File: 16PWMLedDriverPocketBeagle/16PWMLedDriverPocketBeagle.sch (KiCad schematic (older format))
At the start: 16 parts, among them J1 RJ45, J2 RJ45, P1 POCKETBEAGLE-P1, P2 POCKETBEAGLE-P2, T1 + 15 in -, T2 + 15 out -, U1 TCAN332DR, U2 SN65HVD233-HT

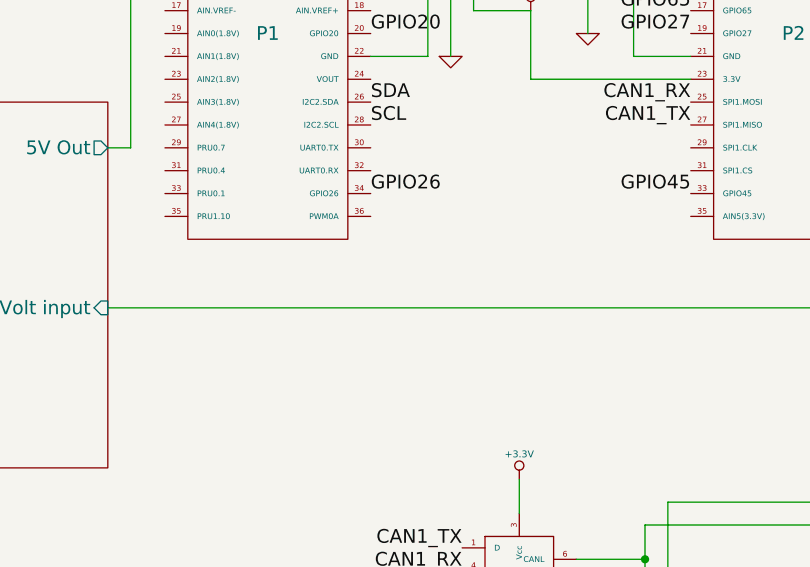
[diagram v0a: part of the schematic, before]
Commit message: Convert the 16PWM Led Drivers to use 12V for the LEDs.
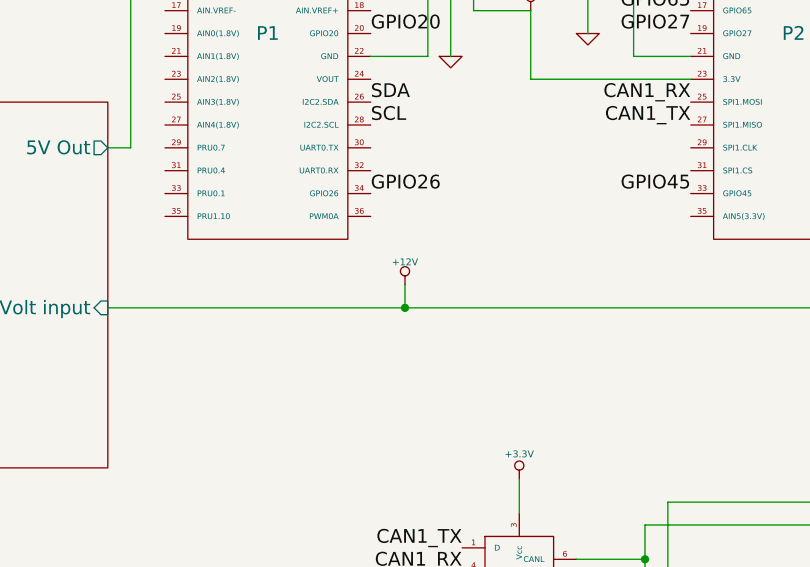
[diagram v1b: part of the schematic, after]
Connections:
- net Power Supply/12-15 Volt input renamed +12V
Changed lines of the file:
@@
 Sheet 1 3
 Title ""
-Date "11 mar 2019"
+Date "28 mar 2019"
 Rev ""
 Comp ""
@@
 	2300 1500 2300 1650
 Connection ~ 2300 1650
+$Comp
+L +12V #PWR014
+U 1 1 5C9CC877
+P 3450 3650
+F 0 "#PWR014" H 3450 3600 20  0001 C CNN
+F 1 "+12V" H 3450 3750 30  0000 C CNN
+F 2 "" H 3450 3650 60  0000 C CNN
+F 3 "" H 3450 3650 60  0000 C CNN
+	1    3450 3650
+	1    0    0    -1
+$EndComp
+Wire Wire Line
+	3450 3650 3450 3750
+Connection ~ 3450 3750
 $EndSCHEMATC

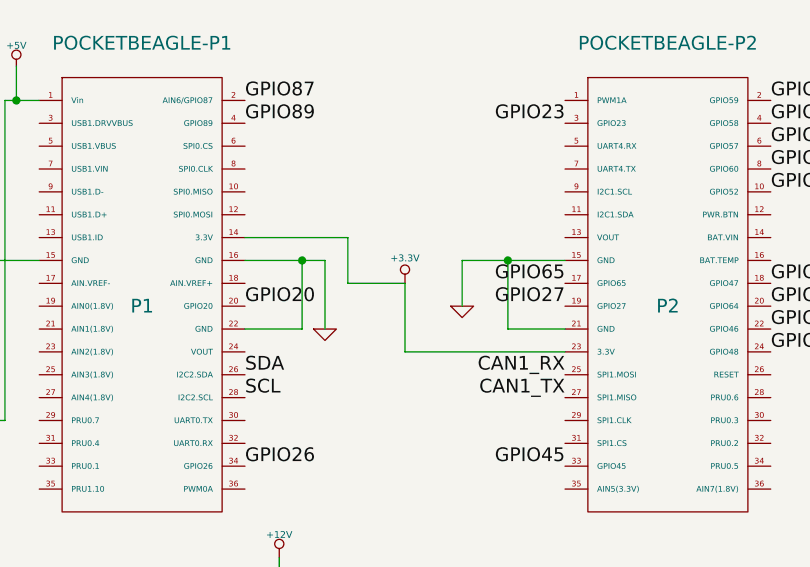
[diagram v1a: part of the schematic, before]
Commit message: Move Pocket Beagle SDA usage from I2C2 to I2C1 (reserved I2C for eeprom?).
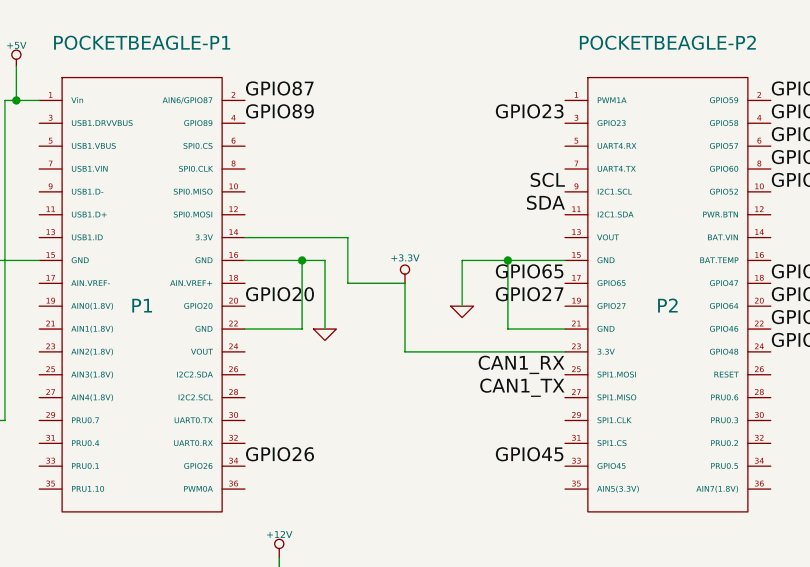
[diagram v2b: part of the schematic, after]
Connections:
- net SCL: now also P2.9 (I2C1.SCL); no longer P1.28 (I2C2.SCL)
- net SDA: now also P2.11 (I2C1.SDA); no longer P1.26 (I2C2.SDA)
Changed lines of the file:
@@
 Sheet 1 3
 Title ""
-Date "28 mar 2019"
+Date "5 jul 2019"
 Rev ""
 Comp ""
@@
 F4 "OE" I L 1700 6850 60
 $EndSheet
-Text Label 3300 2850 0    60   ~ 0
+Text Label 4700 2150 2    60   ~ 0
 SDA
-Text Label 3300 2950 0    60   ~ 0
+Text Label 4700 2050 2    60   ~ 0
 SCL
 Text Label 1700 6300 2    60   ~ 0

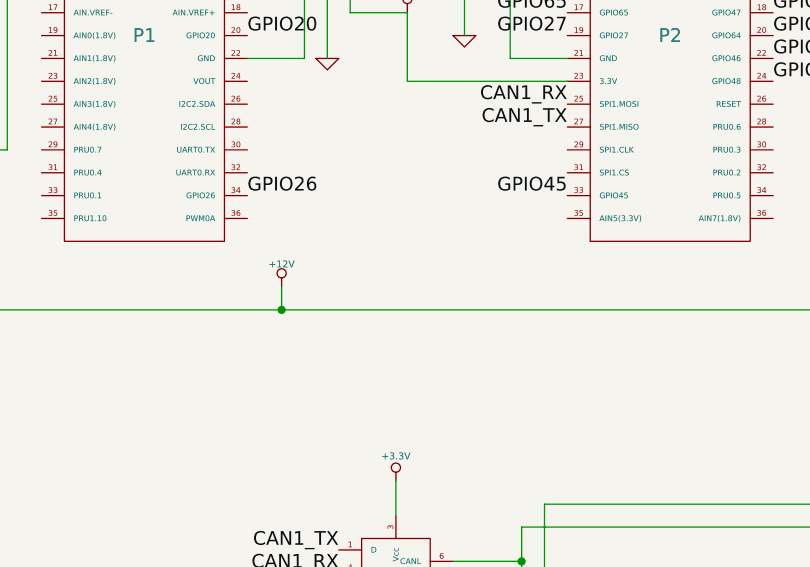
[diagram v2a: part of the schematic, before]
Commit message: Remove unused DIP and add LED power terminals.
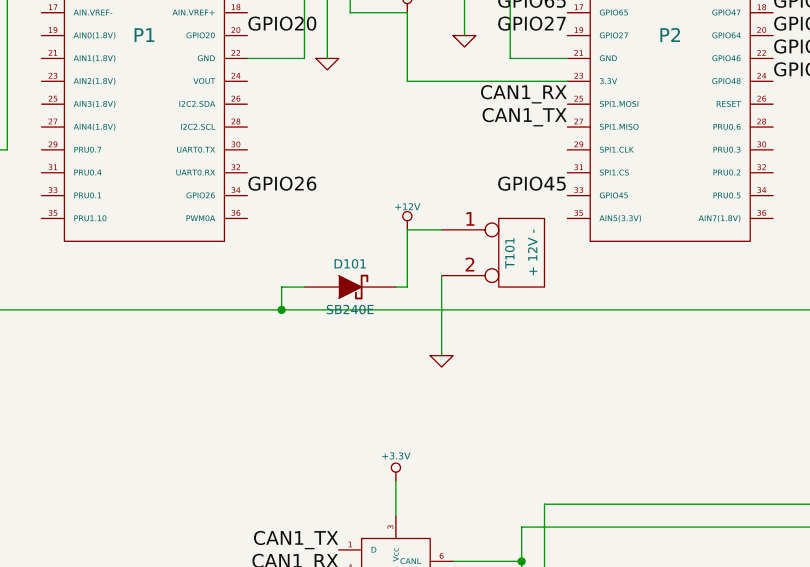
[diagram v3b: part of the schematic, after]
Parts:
- added D101: SB240E, ~, symbol DIODESCH
- added T101: + 12V -, ~, symbol CONN_2
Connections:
- net +12V: now also D101.2 (K), T101.1 (P1); no longer D1.2 (K), D2.1 (A), J1.8, J2.8
- net GND: now also T101.2 (PM)
- new net Power Supply/12-15 Volt input: D1.2 (K), D101.1 (A), D2.1 (A), J1.8, J2.8
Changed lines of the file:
@@
 Sheet 1 3
 Title ""
-Date "5 jul 2019"
+Date "30 jan 2020"
 Rev ""
 Comp ""
@@
 CAN1_TX
 $Comp
-L +3.3V #PWR01
+L +3.3V #PWR108
 U 1 1 5C7C3FF9
 P 4000 2450
-F 0 "#PWR01" H 4000 2410 30  0001 C CNN
+F 0 "#PWR108" H 4000 2410 30  0001 C CNN
 F 1 "+3.3V" H 4000 2560 30  0000 C CNN
 F 2 "" H 4000 2450 60  0000 C CNN
@@
 $EndComp
 $Comp
-L GND #PWR02
+L GND #PWR103
 U 1 1 5C7C401B
 P 3650 2650
-F 0 "#PWR02" H 3650 2650 30  0001 C CNN
+F 0 "#PWR103" H 3650 2650 30  0001 C CNN
 F 1 "GND" H 3650 2580 30  0001 C CNN
 F 2 "" H 3650 2650 60  0000 C CNN
@@
 $EndComp
 $Comp
-L GND #PWR03
+L GND #PWR111
 U 1 1 5C7C4038
 P 4250 2550
-F 0 "#PWR03" H 4250 2550 30  0001 C CNN
+F 0 "#PWR111" H 4250 2550 30  0001 C CNN
 F 1 "GND" H 4250 2480 30  0001 C CNN
 F 2 "" H 4250 2550 60  0000 C CNN
@@
 $EndComp
 $Comp
-L GND #PWR04
+L GND #PWR101
 U 1 1 5C7C406F
 P 2050 2350
-F 0 "#PWR04" H 2050 2350 30  0001 C CNN
+F 0 "#PWR101" H 2050 2350 30  0001 C CNN
 F 1 "GND" H 2050 2280 30  0001 C CNN
 F 2 "" H 2050 2350 60  0000 C CNN
@@
 $EndComp
 $Comp
-L GND #PWR05
+L GND #PWR114
 U 1 1 5C7C42F0
 P 7000 2350
-F 0 "#PWR05" H 7000 2350 30  0001 C CNN
+F 0 "#PWR114" H 7000 2350 30  0001 C CNN
 F 1 "GND" H 7000 2280 30  0001 C CNN
 F 2 "" H 7000 2350 60  0000 C CNN
@@
 CAN1_RX
 $Comp
-L GND #PWR06
+L GND #PWR107
 U 1 1 5C7C44D6
 P 3950 6600
-F 0 "#PWR06" H 3950 6600 30  0001 C CNN
+F 0 "#PWR107" H 3950 6600 30  0001 C CNN
 F 1 "GND" H 3950 6530 30  0001 C CNN
 F 2 "" H 3950 6600 60  0000 C CNN
@@
 $EndComp
 $Comp
-L +3.3V #PWR07
+L +3.3V #PWR106
 U 1 1 5C7C44E5
 P 3950 5650
-F 0 "#PWR07" H 3950 5610 30  0001 C CNN
+F 0 "#PWR106" H 3950 5610 30  0001 C CNN
 F 1 "+3.3V" H 3950 5760 30  0000 C CNN
 F 2 "" H 3950 5650 60  0000 C CNN
@@
 $EndComp
 $Comp
-L +3.3V #PWR08
+L +3.3V #PWR104
 U 1 1 5C7C44F4
 P 3950 4500
-F 0 "#PWR08" H 3950 4460 30  0001 C CNN
+F 0 "#PWR104" H 3950 4460 30  0001 C CNN
 F 1 "+3.3V" H 3950 4610 30  0000 C CNN
 F 2 "" H 3950 4500 60  0000 C CNN
@@
 $EndComp
 $Comp
-L GND #PWR09
+L GND #PWR105
 U 1 1 5C7C4503
 P 3950 5450
-F 0 "#PWR09" H 3950 5450 30  0001 C CNN
+F 0 "#PWR105" H 3950 5450 30  0001 C CNN
 F 1 "GND" H 3950 5380 30  0001 C CNN
 F 2 "" H 3950 5450 60  0000 C CNN
@@
 	4800 5650 5200 5650
 $Comp
-L +3.3V #PWR010
+L +3.3V #PWR112
 U 1 1 5C7C4768
 P 5000 5150
-F 0 "#PWR010" H 5000 5110 30  0001 C CNN
+F 0 "#PWR112" H 5000 5110 30  0001 C CNN
 F 1 "+3.3V" H 5000 5260 30  0000 C CNN
 F 2 "" H 5000 5150 60  0000 C CNN
@@
 $EndComp
 $Comp
-L GND #PWR011
+L GND #PWR113
 U 1 1 5C7C4777
 P 5000 5750
-F 0 "#PWR011" H 5000 5750 30  0001 C CNN
+F 0 "#PWR113" H 5000 5750 30  0001 C CNN
 F 1 "GND" H 5000 5680 30  0001 C CNN
 F 2 "" H 5000 5750 60  0000 C CNN
@@
 $EndComp
 $Comp
-L GND #PWR012
+L GND #PWR115
 U 1 1 5C7C488B
 P 7400 6450
-F 0 "#PWR012" H 7400 6450 30  0001 C CNN
+F 0 "#PWR115" H 7400 6450 30  0001 C CNN
 F 1 "GND" H 7400 6380 30  0001 C CNN
 F 2 "" H 7400 6450 60  0000 C CNN
@@
 GPIO89
 $Comp
-L +5V #PWR013
+L +5V #PWR102
 U 1 1 5C85AC7C
 P 2300 1500
-F 0 "#PWR013" H 2300 1590 20  0001 C CNN
+F 0 "#PWR102" H 2300 1590 20  0001 C CNN
 F 1 "+5V" H 2300 1590 30  0000 C CNN
 F 2 "" H 2300 1500 60  0000 C CNN
@@
 Connection ~ 2300 1650
 $Comp
-L +12V #PWR014
+L +12V #PWR109
 U 1 1 5C9CC877
-P 3450 3650
-F 0 "#PWR014" H 3450 3600 20  0001 C CNN
-F 1 "+12V" H 3450 3750 30  0000 C CNN
-F 2 "" H 3450 3650 60  0000 C CNN
-F 3 "" H 3450 3650 60  0000 C CNN
-	1    3450 3650
+P 4000 3400
+F 0 "#PWR109" H 4000 3350 20  0001 C CNN
+F 1 "+12V" H 4000 3500 30  0000 C CNN
+F 2 "" H 4000 3400 60  0000 C CNN
+F 3 "" H 4000 3400 60  0000 C CNN
+	1    4000 3400
 	1    0    0    -1
 $EndComp
@@
 	3450 3650 3450 3750
 Connection ~ 3450 3750
+$Comp
+L DIODESCH D101
+U 1 1 5E333922
+P 3750 3650
+F 0 "D101" H 3750 3750 40  0000 C CNN
+F 1 "SB240E" H 3750 3550 40  0000 C CNN
+F 2 "~" H 3750 3650 60  0000 C CNN
+F 3 "~" H 3750 3650 60  0000 C CNN
+	1    3750 3650
+	1    0    0    -1
+$EndComp
+Wire Wire Line
+	3450 3650 3550 3650
+Wire Wire Line
+	4000 3650 3950 3650
+Wire Wire Line
+	4000 3400 4000 3650
+$Comp
+L CONN_2 T101
+U 1 1 5E333E44
+P 4500 3500
+F 0 "T101" V 4450 3500 40  0000 C CNN
+F 1 "+ 12V -" V 4550 3500 40  0000 C CNN
+F 2 "~" H 4500 3500 60  0000 C CNN
+F 3 "~" H 4500 3500 60  0000 C CNN
+	1    4500 3500
+	1    0    0    -1
+$EndComp
+Wire Wire Line
+	4150 3400 4000 3400
+$Comp
+L GND #PWR110
+U 1 1 5E333F94
+P 4150 3950
+F 0 "#PWR110" H 4150 3950 30  0001 C CNN
+F 1 "GND" H 4150 3880 30  0001 C CNN
+F 2 "" H 4150 3950 60  0000 C CNN
+F 3 "" H 4150 3950 60  0000 C CNN
+	1    4150 3950
+	1    0    0    -1
+$EndComp
+Wire Wire Line
+	4150 3600 4150 3950
 $EndSCHEMATC
